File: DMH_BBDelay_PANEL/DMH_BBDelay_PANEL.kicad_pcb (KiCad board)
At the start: 2 copper layers, 100 x 200 mm, 38 parts, among them J0 Panel_GND_Solder_Wire_Pad

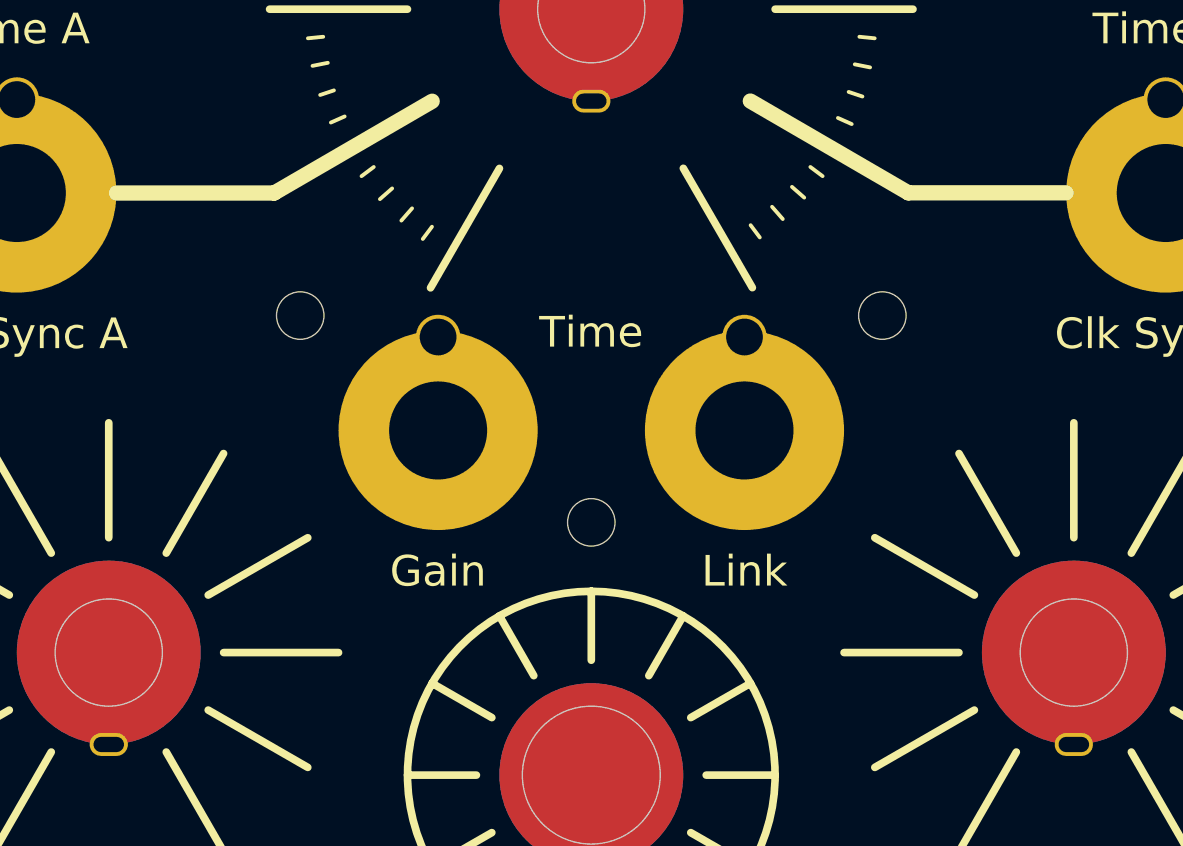
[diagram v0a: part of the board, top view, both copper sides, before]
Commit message: KiCad 10
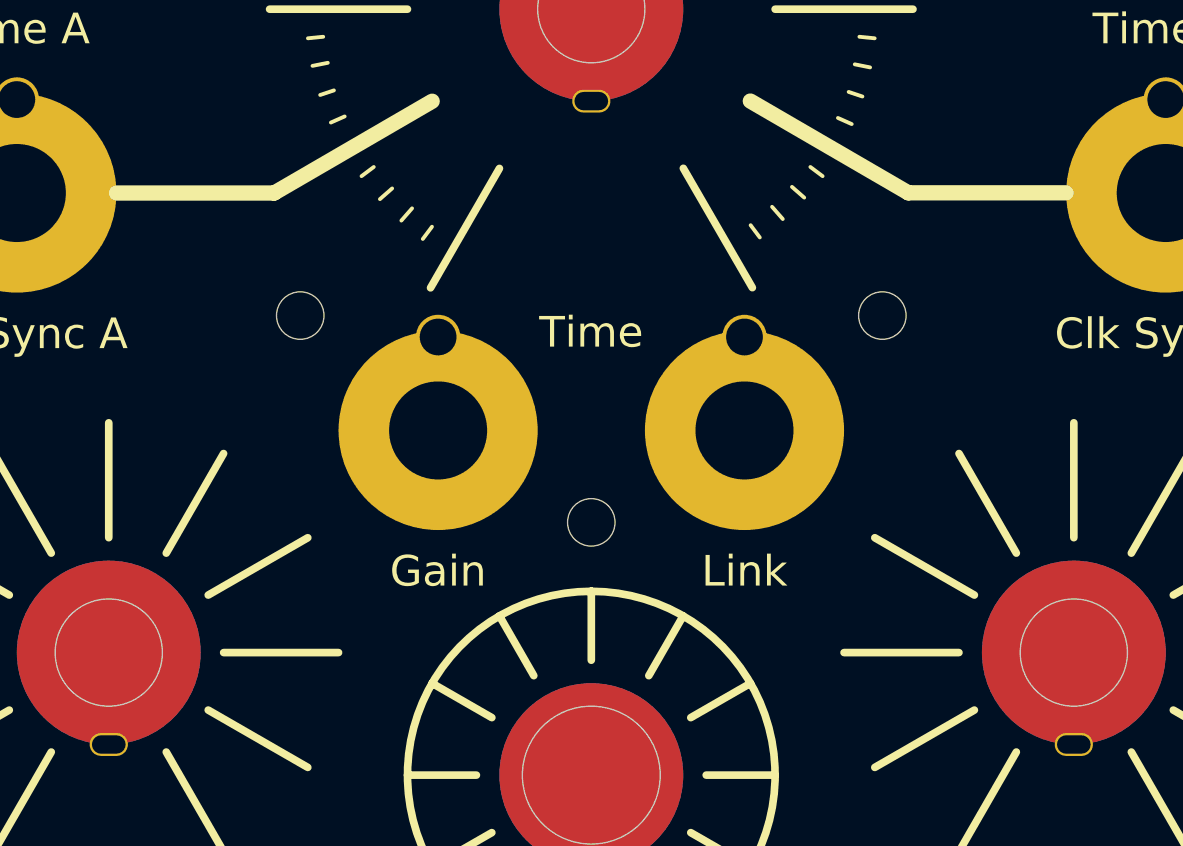
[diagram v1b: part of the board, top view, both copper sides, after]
